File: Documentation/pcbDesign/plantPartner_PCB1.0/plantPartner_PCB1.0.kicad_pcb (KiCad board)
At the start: 2 copper layers, 148.3 x 66.8 mm, 86 parts, among them IC1 MPM3610, J1 Conn_01x04, J10 Screw_Terminal_01x03, J11 Conn_01x02, J12 Conn_01x03, J13 Conn_01x03, J14 Conn_01x03, J15 Conn_01x03, J16 Conn_01x04, J17 Conn_01x03, J18 Screw_Terminal_01x02, J19 Barrel_Jack, J2 Conn_01x04, J20 Conn_02x04_Top_Bottom, J21 Conn_01x04, J22 Conn_01x04, J23 Conn_01x01, J24 Conn_01x03, J25 Conn_01x03, J26 Conn_01x01, J27 Conn_01x01, J28 Conn_01x01, J29 Conn_01x02, J3 Conn_01x04, J30 Screw_Terminal_01x02, J4 Screw_Terminal, J5 Conn_01x02, J6 Screw_Terminal_01x03, J7 Conn_01x03, J8 Conn_02x04_Top_Bottom, J9 Conn_01x03, K1 SRD-05VDC-SL-C, K2 SRD-05VDC-SL-C, Q1 PNP, Q2 PNP, Q4 AO3400A, U1 EL357N-G, U2 MAX485, U3 ESP32-DEVKIT-V1, U4 EL357N-G

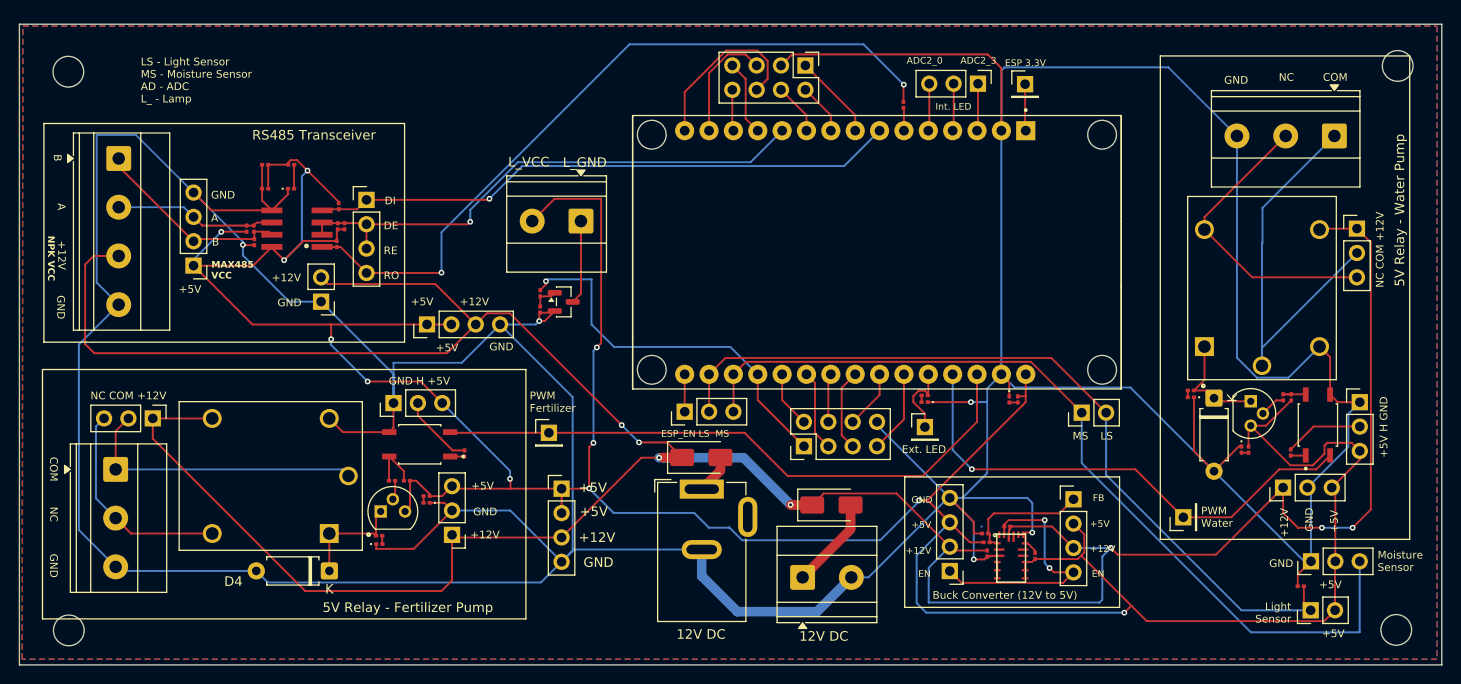
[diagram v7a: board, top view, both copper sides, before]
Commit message: Finalizing some more stuff (grrrr) for JLCPCB printing
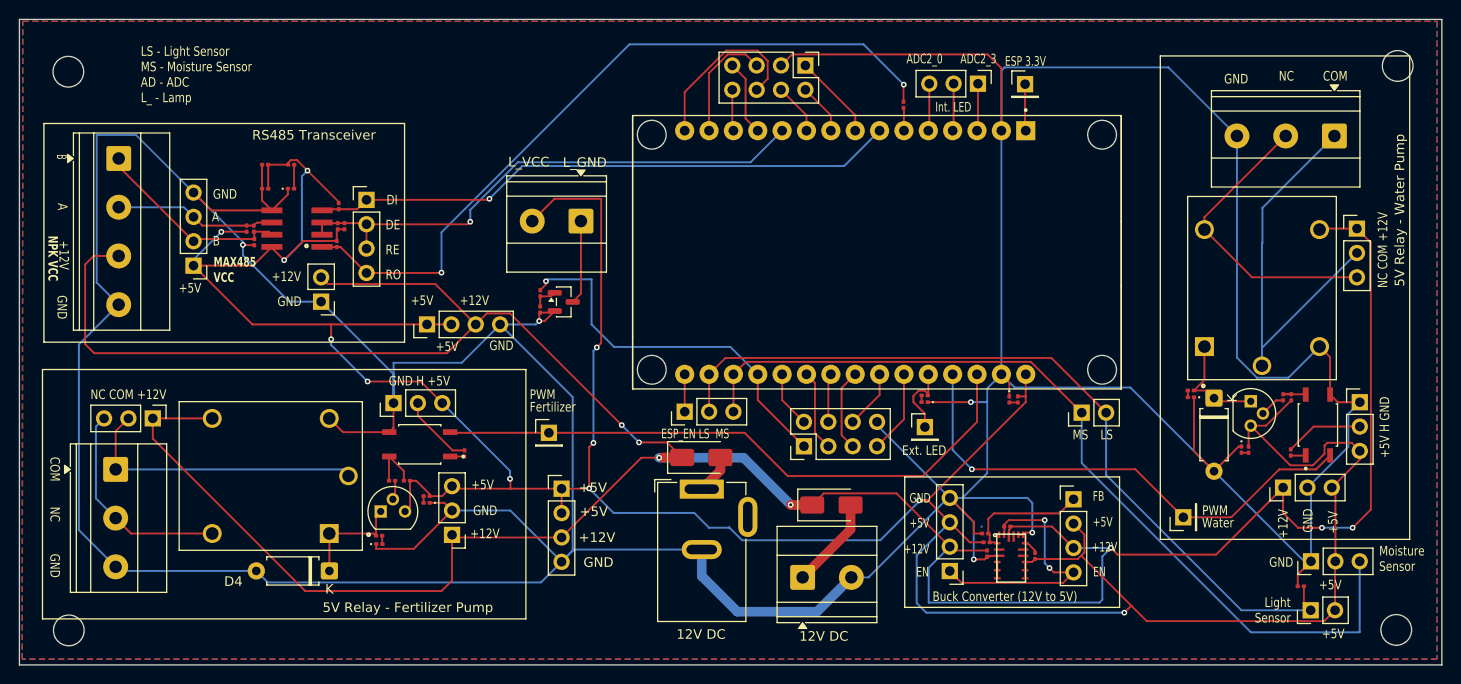
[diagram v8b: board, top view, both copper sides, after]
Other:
- board size 148.3 x 66.8 mm -> 148.3 x 67.3 mm
